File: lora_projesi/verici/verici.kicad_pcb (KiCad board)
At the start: 4 copper layers, 40 x 100 mm, 39 parts, among them J1 USB-C, J2 SMA, SW1 ANA ACMA-KAPAMA, SW2 DUGME 1, SW3 DUGME 2, SW4 DUGME 3, SW5 DUGME 4, SW6 DUGME 5, SW7 DUGME 6, U1 ESP32-S3-WROOM-1-N4, U2 TPS63031DSKR, U3 USBLC6-2SC6, U4 RFM95W-915S2

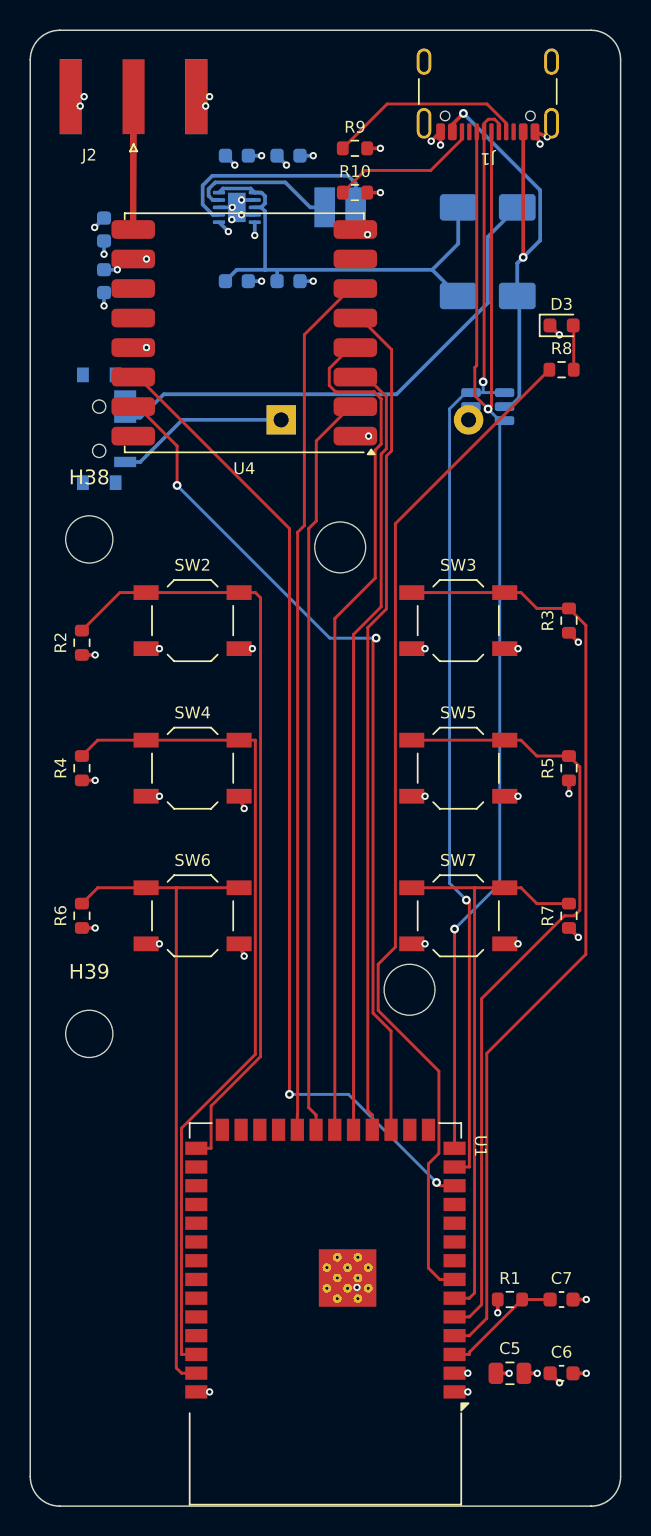
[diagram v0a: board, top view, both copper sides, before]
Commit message: Verici: 4 katmanli kart, DRC temiz, uretim dosyalari, tasarim notu
Co-Authored-By: Claude Sonnet 5.5 <noreply@anthropic.com>
Claude-Session: https://claude.ai/code/session_01Q71gHQtKJ86ZE2CtYTYSwP
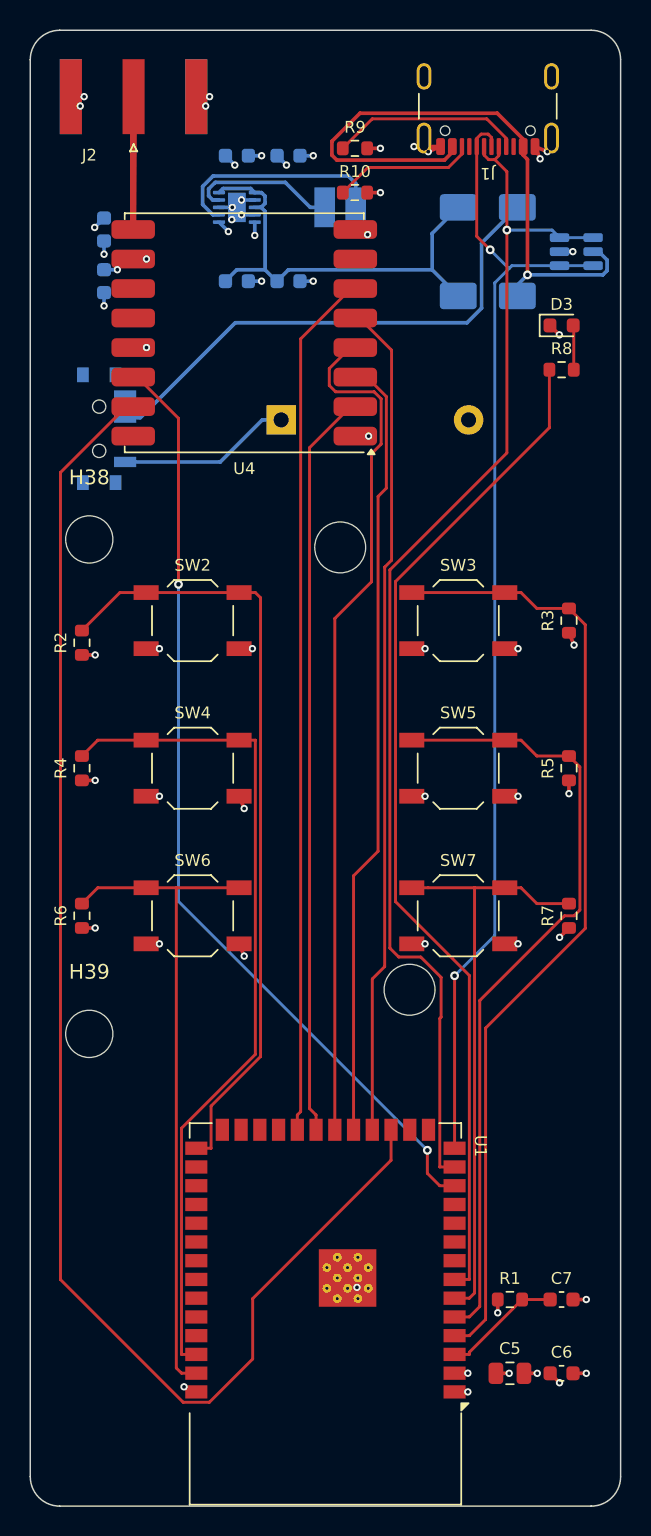
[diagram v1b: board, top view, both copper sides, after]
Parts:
- moved U3 12.1 mm to (37.0, 15.0)
- moved J1 1.00 mm to (31.0, 4.20)
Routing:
- net LORA_DIO1: track 58.4 -> 98.6 mm, vias 2 -> 0
- net USB_DP: track 90.1 -> 78.5 mm
- net VBUS: track 33.4 -> 42.8 mm, vias 2 -> 1
- net USB_DM: track 77.2 -> 83.7 mm, vias 2 -> 1
- net LORA_DIO0: track 66.9 -> 64.6 mm
- net GND: track 37.8 -> 39.6 mm, vias 42 -> 43
- net LED_CTL: track 69.8 -> 69.0 mm

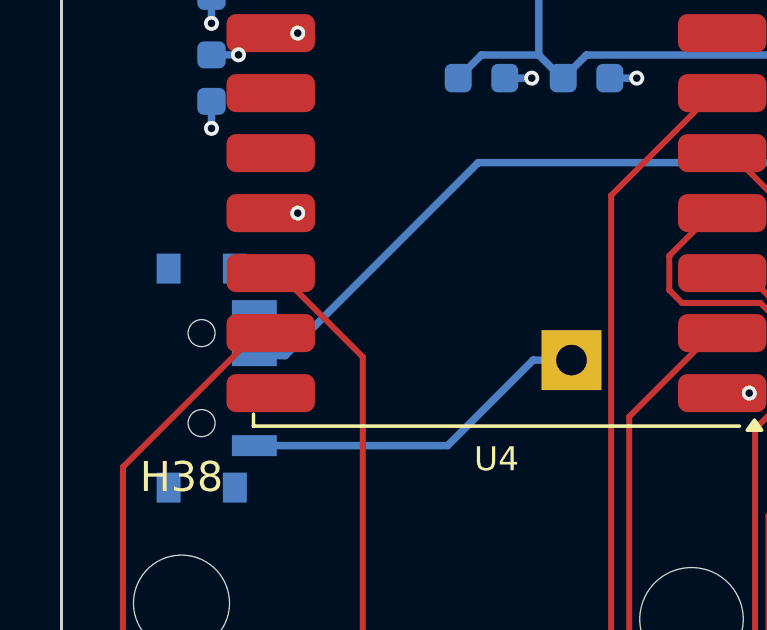
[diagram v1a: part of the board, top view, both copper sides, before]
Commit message: Verici: LORA_DIO0 izi RFM95W ayagina 0,0014 mm yakindi (DRC hatasi), yeniden cizildi; uretim dosyalari yenilendi; veri: denetim sayilari; sema ag etiketleri
Co-Authored-By: Claude Sonnet 5.5 <noreply@anthropic.com>
Claude-Session: https://claude.ai/code/session_01Q71gHQtKJ86ZE2CtYTYSwP
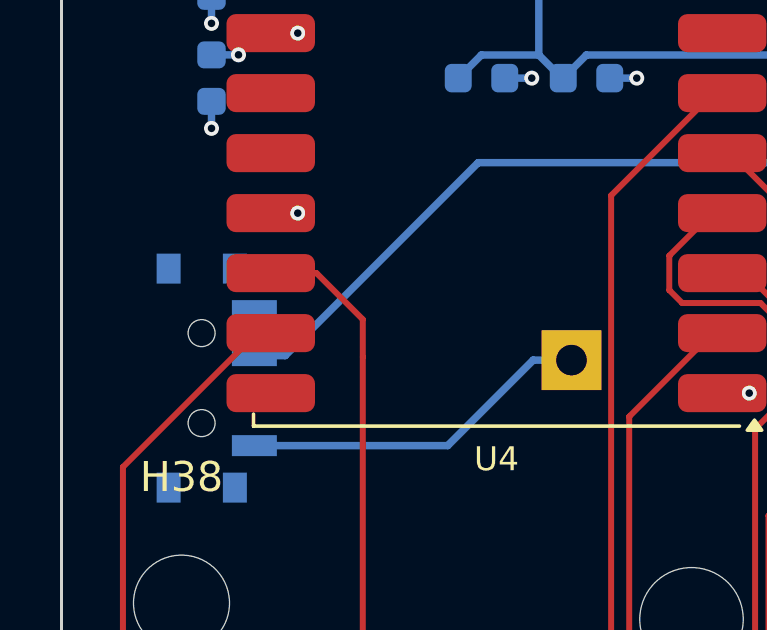
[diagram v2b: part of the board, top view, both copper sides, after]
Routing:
- net LORA_DIO0: track 64.6 -> 65.3 mm
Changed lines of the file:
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@@
   (segment (start 24.7483 37.3513) (end 35.175 26.9246) (width 0.2) (layer "F.Cu") (net 15))
   (segment (start 29.7517 64.044) (end 24.7483 59.0406) (width 0.2) (layer "F.Cu") (net 15))
-  (segment (start 6.975 23.5) (end 7.2506 23.5) (width 0.2) (layer "F.Cu") (net 16))
   (segment (start 10.043 26.2924) (end 10.043 37.539) (width 0.2) (layer "F.Cu") (net 16))
+  (segment (start 10.043 25.043) (end 10.043 26.292) (width 0.2) (layer "F.Cu") (net 16))
+  (segment (start 6.975 23.5) (end 8.5 23.5) (width 0.2) (layer "F.Cu") (net 16))
   (segment (start 27.7483 78.29) (end 26.9067 77.4484) (width 0.2) (layer "F.Cu") (net 16))
+  (segment (start 8.5 23.5) (end 10.043 25.043) (width 0.2) (layer "F.Cu") (net 16))
   (segment (start 28.75 78.29) (end 27.7483 78.29) (width 0.2) (layer "F.Cu") (net 16))
   (segment (start 26.9067 77.4484) (end 26.9067 75.8866) (width 0.2) (layer "F.Cu") (net 16))
-  (segment (start 7.2506 23.5) (end 10.043 26.2924) (width 0.2) (layer "F.Cu") (net 16))
   (via (at 26.9067 75.8866) (size 0.6) (drill 0.3) (layers "F.Cu" "B.Cu") (net 16))
   (via (at 10.043 37.539) (size 0.6) (drill 0.3) (layers "F.Cu" "B.Cu") (net 16))

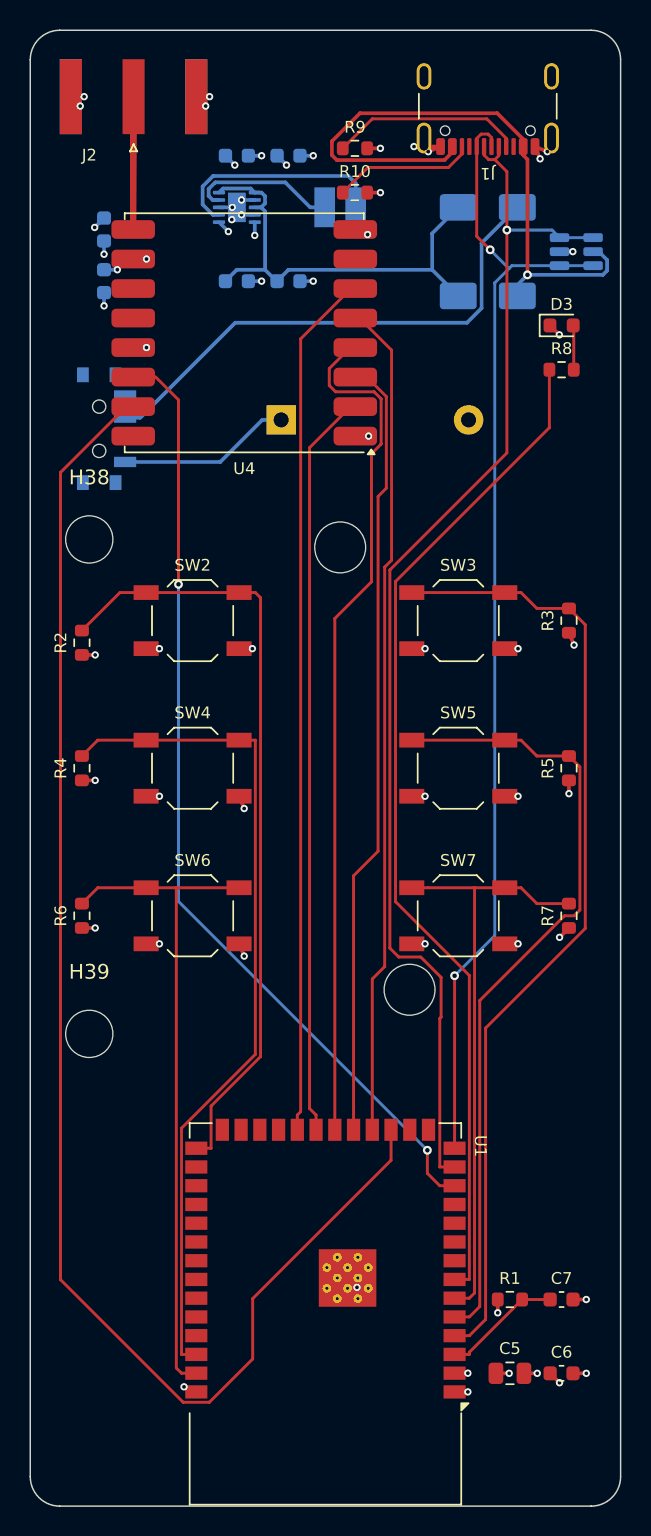
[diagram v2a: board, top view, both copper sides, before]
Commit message: A7670SA, Ra-01H, LM66100 ideal diyot, SRP7028A, USBLC6-2: uretec ve kutuphane (kart yonlendirmesi suruyor)
Co-Authored-By: Claude Sonnet 5.5 <noreply@anthropic.com>
Claude-Session: https://claude.ai/code/session_01Q71gHQtKJ86ZE2CtYTYSwP
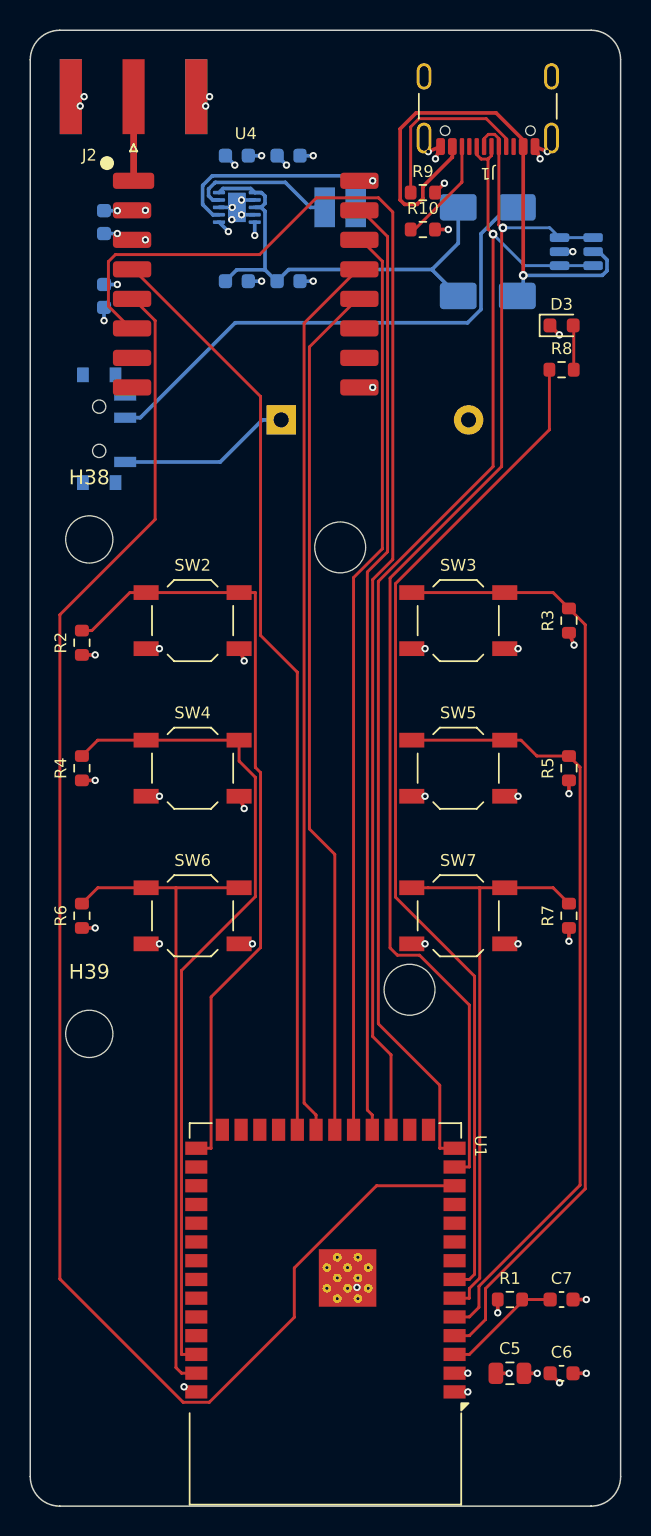
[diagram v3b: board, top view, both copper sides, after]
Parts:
- U4: value RFM95W-915S2 -> Ra-01H; footprint HOPERF_RFM9XW_SMD -> Ra-01H
- moved R9 5.49 mm to (26.6, 11.0)
- moved R10 5.24 mm to (26.6, 13.5)
- moved C9 4.50 mm to (5.00, 18.0)
- moved C8 4.00 mm to (5.00, 13.0)
- moved U4 3.30 mm to (14.6, 17.2), turned to 0 degrees
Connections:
- U4 pad 1: GND -> ANT_RF
- U4 pad 10: GND -> (no net)
- U4 pad 12: (no net) -> LORA_SCK
- U4 pad 13: +3V3 -> LORA_MISO
- U4 pad 14: LORA_DIO0 -> LORA_MOSI
- U4 pad 15: LORA_DIO1 -> LORA_NSS
- U4 pad 16: (no net) -> GND
- U4 pad 2: LORA_MISO -> GND
- U4 pad 3: LORA_MOSI -> +3V3
- U4 pad 4: LORA_SCK -> LORA_RESET
- U4 pad 5: LORA_NSS -> LORA_DIO0
- U4 pad 6: LORA_RESET -> LORA_DIO1
- U4 pad 8: GND -> (no net)
- U4 pad 9: ANT_RF -> GND
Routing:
- net LORA_DIO0: track 65.3 -> 108.0 mm, vias 2 -> 0
- net LORA_MISO: track 50.7 -> 60.2 mm
- net LORA_DIO1: track 98.6 -> 90.0 mm
- net LORA_MOSI: track 53.2 -> 61.8 mm
- net LORA_NSS: track 56.7 -> 63.9 mm
- net ANT_RF: track 18.0 -> 11.4 mm
- net USB_DP: track 78.5 -> 83.2 mm, vias 2 -> 1
- net LORA_RESET: track 58.8 -> 63.0 mm
- net VBUS: track 42.8 -> 39.0 mm
- net CC2: track 9.66 -> 7.22 mm
- net USB_DM: track 83.7 -> 85.2 mm
- net GND: track 39.6 -> 38.7 mm
- net CC1: track 13.0 -> 12.3 mm
- net BTN3: track 56.9 -> 56.2 mm
